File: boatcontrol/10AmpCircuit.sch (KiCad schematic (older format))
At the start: 5 parts, among them K6801 G5RL-K1A-E-DC12, Q6801 T9-818 10A, SW6801 ESB30, SW6802 ESB30

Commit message: More cleanup
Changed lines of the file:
@@
 $Descr A4 11693 8268
 encoding utf-8
-Sheet 69 97
+Sheet 76 97
 Title "Boat Control Hat"
 Date "2020-07-09"
@@
 AR Path="/D1BB8DB4/5F75E923/60474907/D2F4DB55" Ref="D7601"  Part="1"
 AR Path="/D1BB8DB4/5F75E923/60474911/D2F4DB55" Ref="D7701"  Part="1"
-F 0 "D7601" H 4850 4200 50  0000 C CNN
+F 0 "D6801" H 4850 4200 50  0000 C CNN
 F 1 "20mA R/G CA" H 5000 4100 50  0000 C CNN
 F 2 "LED_THT:LED_D5.0mm-3" H 5050 4350 50  0001 C CNN
@@
 AR Path="/D1BB8DB4/5F75E923/60474907/6123E07D" Ref="K7601"  Part="1"
 AR Path="/D1BB8DB4/5F75E923/60474911/6123E07D" Ref="K7701"  Part="1"
-F 0 "K7601" H 6200 4350 50  0000 L CNN
+F 0 "K6801" H 6200 4350 50  0000 L CNN
 F 1 "G5RL-K1A-E-DC12" H 6550 4350 50  0000 L CNN
 F 2 "RELAY_G5RL-K1A-E-DC12" H 6550 4500 50  0001 L BNN
@@
 AR Path="/D1BB8DB4/5F75E923/60474907/D2F4DB59" Ref="SW7601"  Part="1"
 AR Path="/D1BB8DB4/5F75E923/60474911/D2F4DB59" Ref="SW7701"  Part="1"
-F 0 "SW7601" H 3700 3800 50  0000 C CNN
+F 0 "SW6801" H 3700 3800 50  0000 C CNN
 F 1 " ESB30" H 3750 3900 50  0000 C CNN
 F 2 "BoatControl:SW_PUSH_ESB30_DPDT" H 3950 4050 50  0001 C CNN
@@
 AR Path="/D1BB8DB4/5F75E923/60474907/D2F4DB57" Ref="SW7602"  Part="1"
 AR Path="/D1BB8DB4/5F75E923/60474911/D2F4DB57" Ref="SW7702"  Part="1"
-F 0 "SW7602" H 3700 4950 50  0000 C CNN
+F 0 "SW6802" H 3700 4950 50  0000 C CNN
 F 1 " ESB30" H 3750 4850 50  0000 C CNN
 F 2 "BoatControl:SW_PUSH_ESB30_DPDT" H 3950 5100 50  0001 C CNN
@@
 AR Path="/D1BB8DB4/5F75E923/60474907/60DBDD41" Ref="#PWR0141"  Part="1"
 AR Path="/D1BB8DB4/5F75E923/60474911/60DBDD41" Ref="#PWR0143"  Part="1"
-F 0 "#PWR0141" H 5600 4200 50  0001 C CNN
+F 0 "#PWR0135" H 5600 4200 50  0001 C CNN
 F 1 "+12P" H 5615 4523 50  0000 C CNN
 F 2 "" H 5600 4350 50  0001 C CNN
@@
 AR Path="/D1BB8DB4/5F75E923/60474907/60DBDD62" Ref="#PWR0142"  Part="1"
 AR Path="/D1BB8DB4/5F75E923/60474911/60DBDD62" Ref="#PWR0144"  Part="1"
-F 0 "#PWR0142" H 3400 4950 50  0001 C CNN
+F 0 "#PWR0136" H 3400 4950 50  0001 C CNN
 F 1 "GND" H 3405 5027 50  0000 C CNN
 F 2 "" H 3400 5200 50  0001 C CNN
@@
 AR Path="/D1BB8DB4/5F75E923/60474907/D2F4DB58" Ref="Q7601"  Part="1"
 AR Path="/D1BB8DB4/5F75E923/60474911/D2F4DB58" Ref="Q7701"  Part="1"
-F 0 "Q7601" V 6100 3300 50  0000 R CNN
+F 0 "Q6801" V 6100 3300 50  0000 R CNN
 F 1 "T9-818 10A" V 6100 3050 50  0000 R CNN
 F 2 "BoatControl:Schurter_Circuit_Breaker" H 6100 3650 50  0001 C CNN

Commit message: Line up jumpers
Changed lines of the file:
@@
 $Descr A4 11693 8268
 encoding utf-8
-Sheet 76 97
+Sheet 78 97
 Title "Boat Control Hat"
 Date "2020-07-09"
@@
 AR Path="/D1BB8DB4/5F75E923/60474907/D2F4DB55" Ref="D7601"  Part="1"
 AR Path="/D1BB8DB4/5F75E923/60474911/D2F4DB55" Ref="D7701"  Part="1"
-F 0 "D6801" H 4850 4200 50  0000 C CNN
+F 0 "D6701" H 4850 4200 50  0000 C CNN
 F 1 "20mA R/G CA" H 5000 4100 50  0000 C CNN
 F 2 "LED_THT:LED_D5.0mm-3" H 5050 4350 50  0001 C CNN
@@
 AR Path="/D1BB8DB4/5F75E923/60474907/6123E07D" Ref="K7601"  Part="1"
 AR Path="/D1BB8DB4/5F75E923/60474911/6123E07D" Ref="K7701"  Part="1"
-F 0 "K6801" H 6200 4350 50  0000 L CNN
+F 0 "K6701" H 6200 4350 50  0000 L CNN
 F 1 "G5RL-K1A-E-DC12" H 6550 4350 50  0000 L CNN
 F 2 "RELAY_G5RL-K1A-E-DC12" H 6550 4500 50  0001 L BNN
@@
 AR Path="/D1BB8DB4/5F75E923/60474907/D2F4DB59" Ref="SW7601"  Part="1"
 AR Path="/D1BB8DB4/5F75E923/60474911/D2F4DB59" Ref="SW7701"  Part="1"
-F 0 "SW6801" H 3700 3800 50  0000 C CNN
+F 0 "SW6701" H 3700 3800 50  0000 C CNN
 F 1 " ESB30" H 3750 3900 50  0000 C CNN
 F 2 "BoatControl:SW_PUSH_ESB30_DPDT" H 3950 4050 50  0001 C CNN
@@
 AR Path="/D1BB8DB4/5F75E923/60474907/D2F4DB57" Ref="SW7602"  Part="1"
 AR Path="/D1BB8DB4/5F75E923/60474911/D2F4DB57" Ref="SW7702"  Part="1"
-F 0 "SW6802" H 3700 4950 50  0000 C CNN
+F 0 "SW6702" H 3700 4950 50  0000 C CNN
 F 1 " ESB30" H 3750 4850 50  0000 C CNN
 F 2 "BoatControl:SW_PUSH_ESB30_DPDT" H 3950 5100 50  0001 C CNN
@@
 AR Path="/D1BB8DB4/5F75E923/60474907/60DBDD41" Ref="#PWR0141"  Part="1"
 AR Path="/D1BB8DB4/5F75E923/60474911/60DBDD41" Ref="#PWR0143"  Part="1"
-F 0 "#PWR0135" H 5600 4200 50  0001 C CNN
+F 0 "#PWR0141" H 5600 4200 50  0001 C CNN
 F 1 "+12P" H 5615 4523 50  0000 C CNN
 F 2 "" H 5600 4350 50  0001 C CNN
@@
 AR Path="/D1BB8DB4/5F75E923/60474907/60DBDD62" Ref="#PWR0142"  Part="1"
 AR Path="/D1BB8DB4/5F75E923/60474911/60DBDD62" Ref="#PWR0144"  Part="1"
-F 0 "#PWR0136" H 3400 4950 50  0001 C CNN
+F 0 "#PWR0142" H 3400 4950 50  0001 C CNN
 F 1 "GND" H 3405 5027 50  0000 C CNN
 F 2 "" H 3400 5200 50  0001 C CNN
@@
 AR Path="/D1BB8DB4/5F75E923/60474907/D2F4DB58" Ref="Q7601"  Part="1"
 AR Path="/D1BB8DB4/5F75E923/60474911/D2F4DB58" Ref="Q7701"  Part="1"
-F 0 "Q6801" V 6100 3300 50  0000 R CNN
+F 0 "Q6701" V 6100 3300 50  0000 R CNN
 F 1 "T9-818 10A" V 6100 3050 50  0000 R CNN
 F 2 "BoatControl:Schurter_Circuit_Breaker" H 6100 3650 50  0001 C CNN

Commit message: Add Node-RED flows
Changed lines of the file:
@@
 AR Path="/D1BB8DB4/5F75E923/60474907/D2F4DB55" Ref="D7601"  Part="1"
 AR Path="/D1BB8DB4/5F75E923/60474911/D2F4DB55" Ref="D7701"  Part="1"
-F 0 "D6701" H 4850 4200 50  0000 C CNN
+F 0 "D7601" H 4850 4200 50  0000 C CNN
 F 1 "20mA R/G CA" H 5000 4100 50  0000 C CNN
 F 2 "LED_THT:LED_D5.0mm-3" H 5050 4350 50  0001 C CNN
@@
 AR Path="/D1BB8DB4/5F75E923/60474907/6123E07D" Ref="K7601"  Part="1"
 AR Path="/D1BB8DB4/5F75E923/60474911/6123E07D" Ref="K7701"  Part="1"
-F 0 "K6701" H 6200 4350 50  0000 L CNN
+F 0 "K7601" H 6200 4350 50  0000 L CNN
 F 1 "G5RL-K1A-E-DC12" H 6550 4350 50  0000 L CNN
 F 2 "RELAY_G5RL-K1A-E-DC12" H 6550 4500 50  0001 L BNN
@@
 AR Path="/D1BB8DB4/5F75E923/60474907/D2F4DB59" Ref="SW7601"  Part="1"
 AR Path="/D1BB8DB4/5F75E923/60474911/D2F4DB59" Ref="SW7701"  Part="1"
-F 0 "SW6701" H 3700 3800 50  0000 C CNN
+F 0 "SW7601" H 3700 3800 50  0000 C CNN
 F 1 " ESB30" H 3750 3900 50  0000 C CNN
 F 2 "BoatControl:SW_PUSH_ESB30_DPDT" H 3950 4050 50  0001 C CNN
@@
 AR Path="/D1BB8DB4/5F75E923/60474907/D2F4DB57" Ref="SW7602"  Part="1"
 AR Path="/D1BB8DB4/5F75E923/60474911/D2F4DB57" Ref="SW7702"  Part="1"
-F 0 "SW6702" H 3700 4950 50  0000 C CNN
+F 0 "SW7602" H 3700 4950 50  0000 C CNN
 F 1 " ESB30" H 3750 4850 50  0000 C CNN
 F 2 "BoatControl:SW_PUSH_ESB30_DPDT" H 3950 5100 50  0001 C CNN
@@
 AR Path="/D1BB8DB4/5F75E923/60474907/D2F4DB58" Ref="Q7601"  Part="1"
 AR Path="/D1BB8DB4/5F75E923/60474911/D2F4DB58" Ref="Q7701"  Part="1"
-F 0 "Q6701" V 6100 3300 50  0000 R CNN
+F 0 "Q7601" V 6100 3300 50  0000 R CNN
 F 1 "T9-818 10A" V 6100 3050 50  0000 R CNN
 F 2 "BoatControl:Schurter_Circuit_Breaker" H 6100 3650 50  0001 C CNN

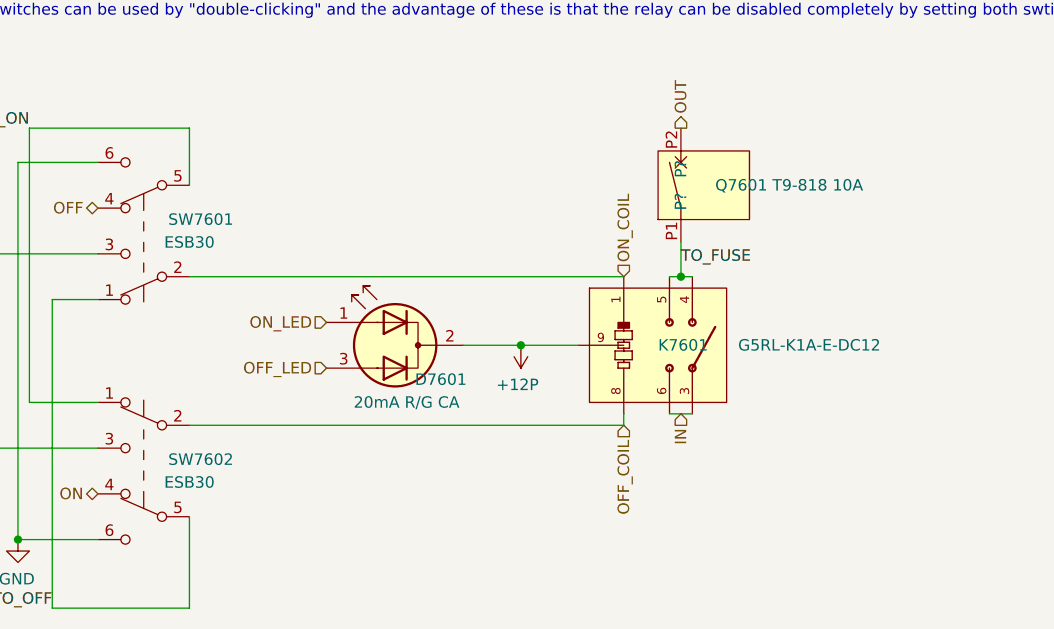
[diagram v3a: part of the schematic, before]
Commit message: Fix SB footprint and symbol
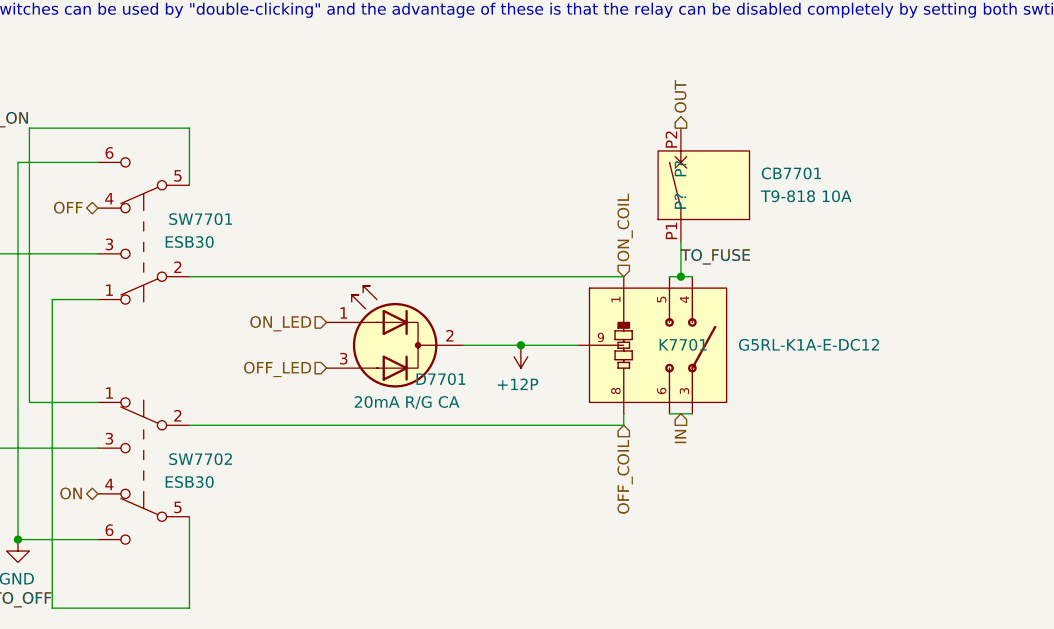
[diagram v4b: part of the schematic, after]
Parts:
- renumbered Q6801 to CB6801
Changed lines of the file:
@@
 $Descr A4 11693 8268
 encoding utf-8
-Sheet 78 97
+Sheet 73 97
 Title "Boat Control Hat"
 Date "2020-07-09"
@@
 AR Path="/D1BB8DB4/5F75E923/60474907/D2F4DB55" Ref="D7601"  Part="1"
 AR Path="/D1BB8DB4/5F75E923/60474911/D2F4DB55" Ref="D7701"  Part="1"
-F 0 "D7601" H 4850 4200 50  0000 C CNN
+F 0 "D7701" H 4850 4200 50  0000 C CNN
 F 1 "20mA R/G CA" H 5000 4100 50  0000 C CNN
 F 2 "LED_THT:LED_D5.0mm-3" H 5050 4350 50  0001 C CNN
@@
 AR Path="/D1BB8DB4/5F75E923/60474907/6123E07D" Ref="K7601"  Part="1"
 AR Path="/D1BB8DB4/5F75E923/60474911/6123E07D" Ref="K7701"  Part="1"
-F 0 "K7601" H 6200 4350 50  0000 L CNN
+F 0 "K7701" H 6200 4350 50  0000 L CNN
 F 1 "G5RL-K1A-E-DC12" H 6550 4350 50  0000 L CNN
 F 2 "RELAY_G5RL-K1A-E-DC12" H 6550 4500 50  0001 L BNN
@@
 AR Path="/D1BB8DB4/5F75E923/60474907/D2F4DB59" Ref="SW7601"  Part="1"
 AR Path="/D1BB8DB4/5F75E923/60474911/D2F4DB59" Ref="SW7701"  Part="1"
-F 0 "SW7601" H 3700 3800 50  0000 C CNN
+F 0 "SW7701" H 3700 3800 50  0000 C CNN
 F 1 " ESB30" H 3750 3900 50  0000 C CNN
 F 2 "BoatControl:SW_PUSH_ESB30_DPDT" H 3950 4050 50  0001 C CNN
@@
 AR Path="/D1BB8DB4/5F75E923/60474907/D2F4DB57" Ref="SW7602"  Part="1"
 AR Path="/D1BB8DB4/5F75E923/60474911/D2F4DB57" Ref="SW7702"  Part="1"
-F 0 "SW7602" H 3700 4950 50  0000 C CNN
+F 0 "SW7702" H 3700 4950 50  0000 C CNN
 F 1 " ESB30" H 3750 4850 50  0000 C CNN
 F 2 "BoatControl:SW_PUSH_ESB30_DPDT" H 3950 5100 50  0001 C CNN
@@
 AR Path="/D16552B4/5FA17F86/81A9CCA4/D2F4DB58" Ref="Q?"  Part="1"
 AR Path="/D16552B4/5FA17F86/81A9CC9C/D2F4DB58" Ref="Q?"  Part="1"
-AR Path="/D1BB8DB4/5F76AF55/60474911/D2F4DB58" Ref="Q6801"  Part="1"
-AR Path="/D1BB8DB4/5F76AF55/60474907/D2F4DB58" Ref="Q6701"  Part="1"
-AR Path="/D1BB8DB4/5F75E923/60474907/D2F4DB58" Ref="Q7601"  Part="1"
-AR Path="/D1BB8DB4/5F75E923/60474911/D2F4DB58" Ref="Q7701"  Part="1"
-F 0 "Q7601" V 6100 3300 50  0000 R CNN
-F 1 "T9-818 10A" V 6100 3050 50  0000 R CNN
+AR Path="/D1BB8DB4/5F76AF55/60474911/D2F4DB58" Ref="CB6801"  Part="1"
+AR Path="/D1BB8DB4/5F76AF55/60474907/D2F4DB58" Ref="CB6701"  Part="1"
+AR Path="/D1BB8DB4/5F75E923/60474907/D2F4DB58" Ref="CB7601"  Part="1"
+AR Path="/D1BB8DB4/5F75E923/60474911/D2F4DB58" Ref="CB7701"  Part="1"
+F 0 "CB7701" V 6150 3100 50  0000 R CNN
+F 1 "T9-818 10A" V 6050 3100 50  0000 R CNN
 F 2 "BoatControl:Schurter_Circuit_Breaker" H 6100 3650 50  0001 C CNN
 F 3 "https://eu.mouser.com/datasheet/2/358/typ_T9-818-1276014.pdf" H 6100 3650 50  0001 C CNN

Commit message: Cleanup
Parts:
- D6801: symbol Device:LED_Dual_ACA -> boatcontrol-rescue:LED_Dual_ACA-Device
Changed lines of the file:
@@
 $EndDescr
 $Comp
-L Device:LED_Dual_ACA D?
+L boatcontrol-rescue:LED_Dual_ACA-Device D?
 U 1 1 D2F4DB55
 P 5050 4350
@@
 AR Path="/D1BB8DB4/5F75E923/60474907/D2F4DB55" Ref="D7601"  Part="1"
 AR Path="/D1BB8DB4/5F75E923/60474911/D2F4DB55" Ref="D7701"  Part="1"
-F 0 "D7701" H 4850 4200 50  0000 C CNN
+F 0 "D7601" H 4850 4200 50  0000 C CNN
 F 1 "20mA R/G CA" H 5000 4100 50  0000 C CNN
 F 2 "LED_THT:LED_D5.0mm-3" H 5050 4350 50  0001 C CNN
@@
 AR Path="/D1BB8DB4/5F75E923/60474907/6123E07D" Ref="K7601"  Part="1"
 AR Path="/D1BB8DB4/5F75E923/60474911/6123E07D" Ref="K7701"  Part="1"
-F 0 "K7701" H 6200 4350 50  0000 L CNN
+F 0 "K7601" H 6200 4350 50  0000 L CNN
 F 1 "G5RL-K1A-E-DC12" H 6550 4350 50  0000 L CNN
 F 2 "RELAY_G5RL-K1A-E-DC12" H 6550 4500 50  0001 L BNN
@@
 AR Path="/D1BB8DB4/5F75E923/60474907/D2F4DB59" Ref="SW7601"  Part="1"
 AR Path="/D1BB8DB4/5F75E923/60474911/D2F4DB59" Ref="SW7701"  Part="1"
-F 0 "SW7701" H 3700 3800 50  0000 C CNN
+F 0 "SW7601" H 3700 3800 50  0000 C CNN
 F 1 " ESB30" H 3750 3900 50  0000 C CNN
 F 2 "BoatControl:SW_PUSH_ESB30_DPDT" H 3950 4050 50  0001 C CNN
@@
 AR Path="/D1BB8DB4/5F75E923/60474907/D2F4DB57" Ref="SW7602"  Part="1"
 AR Path="/D1BB8DB4/5F75E923/60474911/D2F4DB57" Ref="SW7702"  Part="1"
-F 0 "SW7702" H 3700 4950 50  0000 C CNN
+F 0 "SW7602" H 3700 4950 50  0000 C CNN
 F 1 " ESB30" H 3750 4850 50  0000 C CNN
 F 2 "BoatControl:SW_PUSH_ESB30_DPDT" H 3950 5100 50  0001 C CNN
@@
 AR Path="/D1BB8DB4/5F75E923/60474907/D2F4DB58" Ref="CB7601"  Part="1"
 AR Path="/D1BB8DB4/5F75E923/60474911/D2F4DB58" Ref="CB7701"  Part="1"
-F 0 "CB7701" V 6150 3100 50  0000 R CNN
+F 0 "CB7601" V 6150 3100 50  0000 R CNN
 F 1 "T9-818 10A" V 6050 3100 50  0000 R CNN
 F 2 "BoatControl:Schurter_Circuit_Breaker" H 6100 3650 50  0001 C CNN

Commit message: Fits
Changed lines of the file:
@@
 $Descr A4 11693 8268
 encoding utf-8
-Sheet 73 97
+Sheet 56 97
 Title "Boat Control Hat"
 Date "2020-07-09"
@@
 AR Path="/D1BB8DB4/5F75E923/60474907/D2F4DB55" Ref="D7601"  Part="1"
 AR Path="/D1BB8DB4/5F75E923/60474911/D2F4DB55" Ref="D7701"  Part="1"
-F 0 "D7601" H 4850 4200 50  0000 C CNN
+F 0 "D6701" H 4850 4200 50  0000 C CNN
 F 1 "20mA R/G CA" H 5000 4100 50  0000 C CNN
 F 2 "LED_THT:LED_D5.0mm-3" H 5050 4350 50  0001 C CNN
@@
 AR Path="/D1BB8DB4/5F75E923/60474907/6123E07D" Ref="K7601"  Part="1"
 AR Path="/D1BB8DB4/5F75E923/60474911/6123E07D" Ref="K7701"  Part="1"
-F 0 "K7601" H 6200 4350 50  0000 L CNN
+F 0 "K6701" H 6200 4350 50  0000 L CNN
 F 1 "G5RL-K1A-E-DC12" H 6550 4350 50  0000 L CNN
 F 2 "RELAY_G5RL-K1A-E-DC12" H 6550 4500 50  0001 L BNN
@@
 AR Path="/D1BB8DB4/5F75E923/60474907/D2F4DB59" Ref="SW7601"  Part="1"
 AR Path="/D1BB8DB4/5F75E923/60474911/D2F4DB59" Ref="SW7701"  Part="1"
-F 0 "SW7601" H 3700 3800 50  0000 C CNN
+F 0 "SW6701" H 3700 3800 50  0000 C CNN
 F 1 " ESB30" H 3750 3900 50  0000 C CNN
 F 2 "BoatControl:SW_PUSH_ESB30_DPDT" H 3950 4050 50  0001 C CNN
@@
 AR Path="/D1BB8DB4/5F75E923/60474907/D2F4DB57" Ref="SW7602"  Part="1"
 AR Path="/D1BB8DB4/5F75E923/60474911/D2F4DB57" Ref="SW7702"  Part="1"
-F 0 "SW7602" H 3700 4950 50  0000 C CNN
+F 0 "SW6702" H 3700 4950 50  0000 C CNN
 F 1 " ESB30" H 3750 4850 50  0000 C CNN
 F 2 "BoatControl:SW_PUSH_ESB30_DPDT" H 3950 5100 50  0001 C CNN
@@
 AR Path="/D1BB8DB4/5F75E923/60474907/D2F4DB58" Ref="CB7601"  Part="1"
 AR Path="/D1BB8DB4/5F75E923/60474911/D2F4DB58" Ref="CB7701"  Part="1"
-F 0 "CB7601" V 6150 3100 50  0000 R CNN
+F 0 "CB6701" V 6150 3100 50  0000 R CNN
 F 1 "T9-818 10A" V 6050 3100 50  0000 R CNN
 F 2 "BoatControl:Schurter_Circuit_Breaker" H 6100 3650 50  0001 C CNN

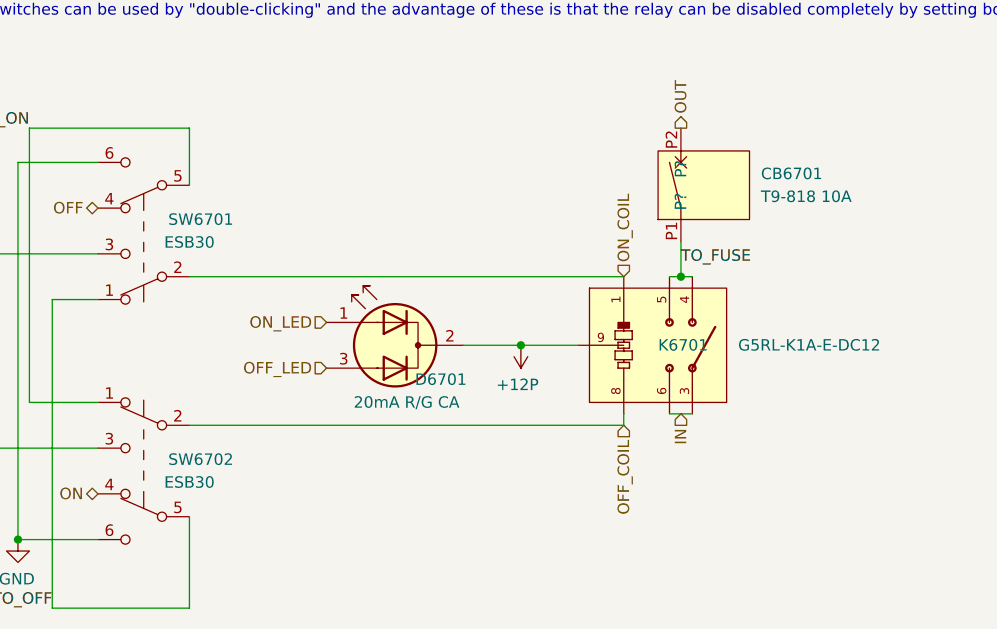
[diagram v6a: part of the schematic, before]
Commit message: Fix silkscreen logos and graphics
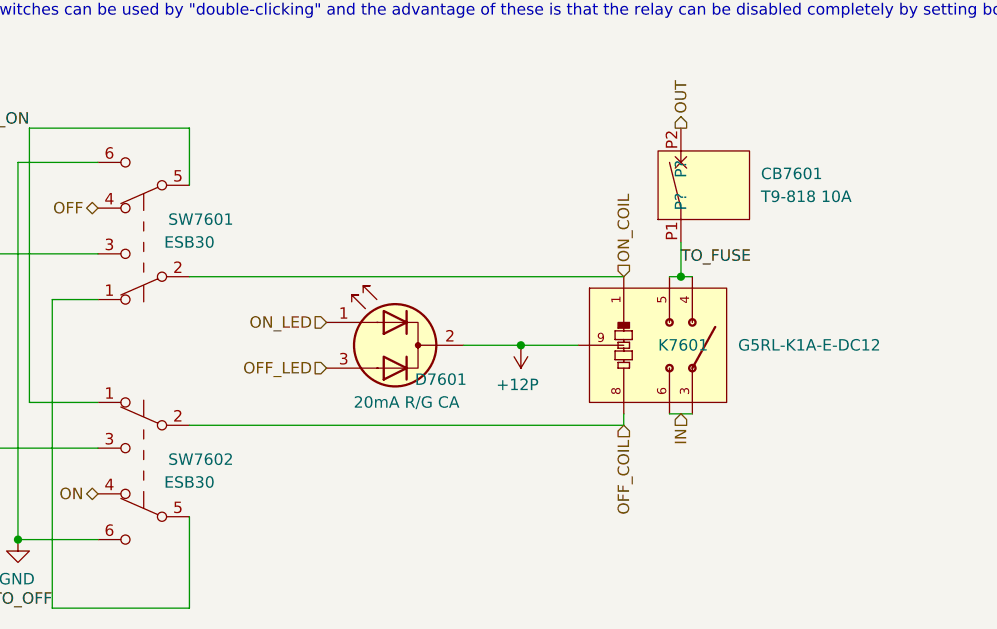
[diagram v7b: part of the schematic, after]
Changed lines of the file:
@@
 AR Path="/D1BB8DB4/5F75E923/60474907/D2F4DB55" Ref="D7601"  Part="1"
 AR Path="/D1BB8DB4/5F75E923/60474911/D2F4DB55" Ref="D7701"  Part="1"
-F 0 "D6701" H 4850 4200 50  0000 C CNN
+F 0 "D7601" H 4850 4200 50  0000 C CNN
 F 1 "20mA R/G CA" H 5000 4100 50  0000 C CNN
 F 2 "LED_THT:LED_D5.0mm-3" H 5050 4350 50  0001 C CNN
@@
 AR Path="/D1BB8DB4/5F75E923/60474907/6123E07D" Ref="K7601"  Part="1"
 AR Path="/D1BB8DB4/5F75E923/60474911/6123E07D" Ref="K7701"  Part="1"
-F 0 "K6701" H 6200 4350 50  0000 L CNN
+F 0 "K7601" H 6200 4350 50  0000 L CNN
 F 1 "G5RL-K1A-E-DC12" H 6550 4350 50  0000 L CNN
 F 2 "RELAY_G5RL-K1A-E-DC12" H 6550 4500 50  0001 L BNN
@@
 AR Path="/D1BB8DB4/5F75E923/60474907/D2F4DB59" Ref="SW7601"  Part="1"
 AR Path="/D1BB8DB4/5F75E923/60474911/D2F4DB59" Ref="SW7701"  Part="1"
-F 0 "SW6701" H 3700 3800 50  0000 C CNN
+F 0 "SW7601" H 3700 3800 50  0000 C CNN
 F 1 " ESB30" H 3750 3900 50  0000 C CNN
 F 2 "BoatControl:SW_PUSH_ESB30_DPDT" H 3950 4050 50  0001 C CNN
@@
 AR Path="/D1BB8DB4/5F75E923/60474907/D2F4DB57" Ref="SW7602"  Part="1"
 AR Path="/D1BB8DB4/5F75E923/60474911/D2F4DB57" Ref="SW7702"  Part="1"
-F 0 "SW6702" H 3700 4950 50  0000 C CNN
+F 0 "SW7602" H 3700 4950 50  0000 C CNN
 F 1 " ESB30" H 3750 4850 50  0000 C CNN
 F 2 "BoatControl:SW_PUSH_ESB30_DPDT" H 3950 5100 50  0001 C CNN
@@
 AR Path="/D1BB8DB4/5F75E923/60474907/D2F4DB58" Ref="CB7601"  Part="1"
 AR Path="/D1BB8DB4/5F75E923/60474911/D2F4DB58" Ref="CB7701"  Part="1"
-F 0 "CB6701" V 6150 3100 50  0000 R CNN
+F 0 "CB7601" V 6150 3100 50  0000 R CNN
 F 1 "T9-818 10A" V 6050 3100 50  0000 R CNN
 F 2 "BoatControl:Schurter_Circuit_Breaker" H 6100 3650 50  0001 C CNN

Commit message: Fix rescued symbols
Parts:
- D6801: symbol boatcontrol-rescue:LED_Dual_ACA-Device -> Device:LED_Dual_AKA
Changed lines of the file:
@@
 $EndDescr
 $Comp
-L boatcontrol-rescue:LED_Dual_ACA-Device D?
+L Device:LED_Dual_AKA D?
 U 1 1 D2F4DB55
 P 5050 4350
